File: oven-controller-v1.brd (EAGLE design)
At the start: 61 x 57.1 mm, 22 parts, among them Q1 IRFL310, U1 ARDUINO_SHIELDLONGPADS

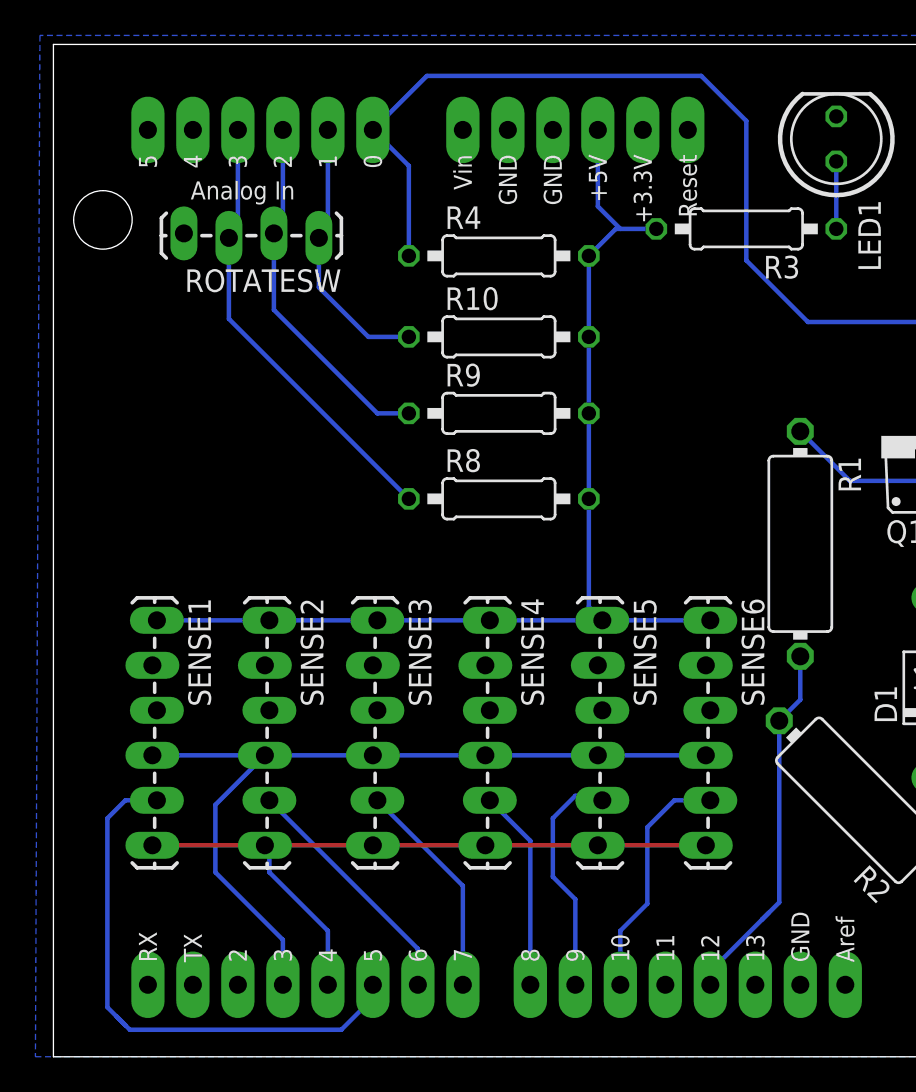
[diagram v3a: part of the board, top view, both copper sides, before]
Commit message: Final board routed.
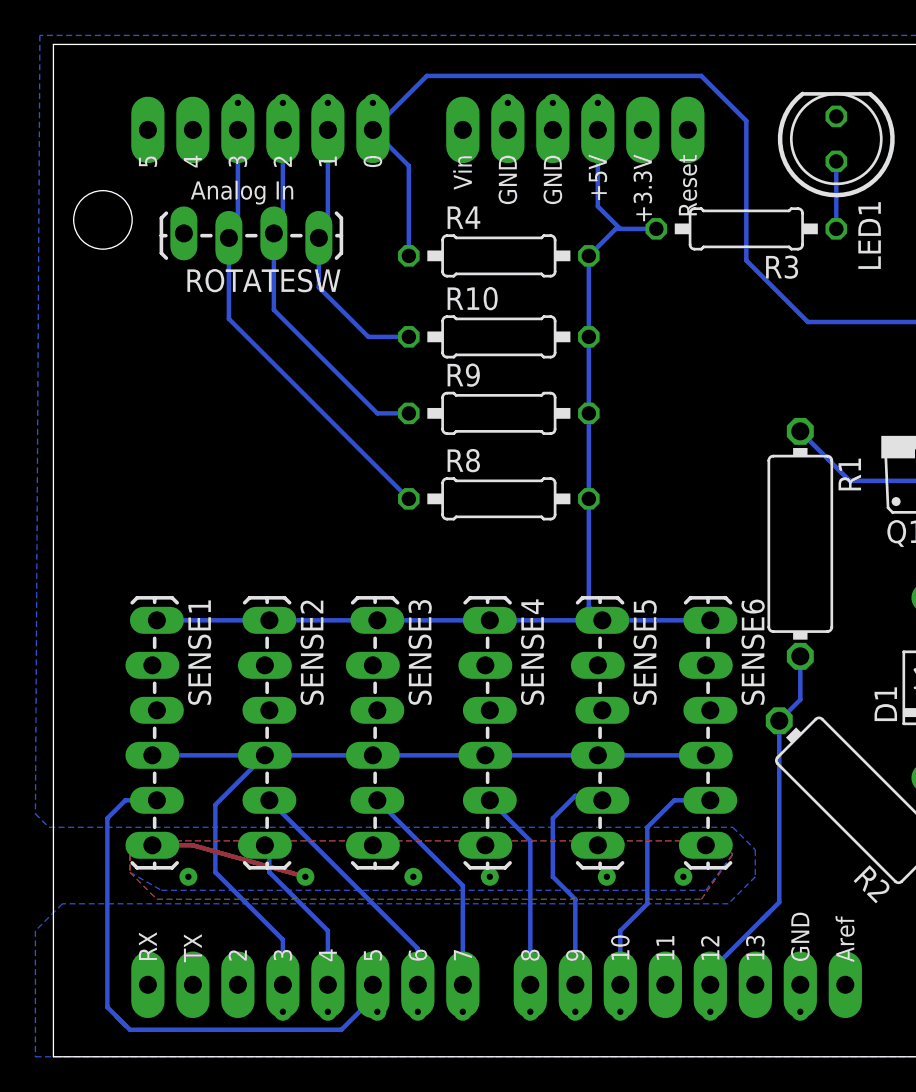
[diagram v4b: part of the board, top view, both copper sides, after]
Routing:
- net SCLK_PIN4: track 40.8 -> 20.0 mm, vias 0 -> 7
- net A1: track 15.3 -> 16.9 mm, vias 0 -> 1
- net SDA_PIN3: track 46.9 -> 48.5 mm, vias 0 -> 1
- net PIN12: track 21.2 -> 22.7 mm, vias 0 -> 1
- net CS_PIN9: track 13.3 -> 14.9 mm, vias 0 -> 1
- net CS_PIN8: track 11.4 -> 12.9 mm, vias 0 -> 1
- net CS_PIN7: track 12.4 -> 13.9 mm, vias 0 -> 1
- net A3: track 25.2 -> 26.8 mm, vias 0 -> 1
- net A2: track 20.4 -> 21.9 mm, vias 0 -> 1
- net A0: track 55.9 -> 57.4 mm, vias 0 -> 1
- net 5V: track 62.7 -> 64.2 mm, vias 0 -> 1
- net CS_PIN6: track 13.9 -> 15.4 mm, vias 0 -> 1
- net CS_PIN10: track 13.7 -> 15.2 mm, vias 0 -> 1
- net CS_PIN5: track 31.6 -> 32.6 mm, vias 0 -> 1
- added copper zone on layer 1, net SCLK_PIN4
- added copper zone on layer 16, net SCLK_PIN4
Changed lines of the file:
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@@
 <grid distance="0.01" unitdist="inch" unit="inch" style="dots" multiple="1" display="yes" altdistance="0.001" altunitdist="inch" altunit="inch"/>
 <layers>
-<layer number="1" name="Top" color="4" fill="1" visible="yes" active="yes"/>
+<layer number="1" name="Top" color="4" fill="1" visible="no" active="yes"/>
 <layer number="2" name="Route2" color="1" fill="3" visible="no" active="no"/>
 <layer number="3" name="Route3" color="4" fill="3" visible="no" active="no"/>
@@
 <vertex x="61.214" y="57.658"/>
 <vertex x="-0.762" y="57.658"/>
+<vertex x="-1.016" y="13.716"/>
+<vertex x="-0.254" y="12.954"/>
+<vertex x="38.354" y="12.954"/>
+<vertex x="39.624" y="11.684"/>
+<vertex x="39.624" y="10.16"/>
+<vertex x="38.1" y="8.636"/>
+<vertex x="0.508" y="8.636"/>
+<vertex x="-1.016" y="7.112"/>
 <vertex x="-1.016" y="0"/>
 <vertex x="60.96" y="0"/>
 </polygon>
+<via x="25.654" y="53.848" extent="1-16" drill="0.3556" diameter="1.016"/>
+<via x="28.194" y="53.848" extent="1-16" drill="0.3556" diameter="1.016"/>
+<via x="42.164" y="2.54" extent="1-16" drill="0.3556" diameter="1.016"/>
 </signal>
 <signal name="PIN12">
@@
 <wire x1="40.975871875" y1="18.968125" x2="40.975871875" y2="8.717871875" width="0.254" layer="16"/>
 <wire x1="40.975871875" y1="8.717871875" x2="40.005" y2="7.747" width="0.254" layer="16"/>
+<via x="37.084" y="2.54" extent="1-16" drill="0.3556" diameter="1.016"/>
+<wire x1="37.084" y1="2.54" x2="37.084" y2="4.064" width="0.254" layer="16"/>
 </signal>
 <signal name="N$2">
@@
 <wire x1="24.384" y1="17.018" x2="30.734" y2="17.018" width="0.254" layer="16"/>
 <wire x1="30.734" y1="17.018" x2="36.83" y2="17.018" width="0.254" layer="16"/>
+<via x="12.954" y="2.54" extent="1-16" drill="0.3556" diameter="1.016"/>
+<wire x1="12.954" y1="2.54" x2="12.954" y2="4.064" width="0.254" layer="16"/>
 </signal>
 <signal name="SCLK_PIN4">
@@
 <contactref element="SENSE6" pad="6"/>
 <contactref element="U1" pad="D4"/>
-<wire x1="5.588" y1="11.938" x2="11.938" y2="11.938" width="0.254" layer="1"/>
-<wire x1="11.938" y1="11.938" x2="18.034" y2="11.938" width="0.254" layer="1"/>
-<wire x1="18.034" y1="11.938" x2="24.384" y2="11.938" width="0.254" layer="1"/>
-<wire x1="24.384" y1="11.938" x2="30.734" y2="11.938" width="0.254" layer="1"/>
 <wire x1="30.734" y1="11.938" x2="30.988" y2="11.938" width="0.254" layer="1"/>
-<wire x1="30.734" y1="11.938" x2="36.83" y2="11.938" width="0.254" layer="1"/>
 <wire x1="15.494" y1="4.064" x2="15.494" y2="7.112" width="0.254" layer="16"/>
 <wire x1="15.494" y1="7.112" x2="12.192" y2="10.414" width="0.254" layer="16"/>
 <wire x1="12.192" y1="10.414" x2="12.192" y2="11.684" width="0.254" layer="16"/>
 <wire x1="12.192" y1="11.684" x2="11.938" y2="11.938" width="0.254" layer="16"/>
+<polygon width="0.254" layer="1">
+<vertex x="4.318" y="11.938"/>
+<vertex x="4.318" y="10.414"/>
+<vertex x="5.842" y="8.89"/>
+<vertex x="36.576" y="8.89"/>
+<vertex x="38.354" y="11.43"/>
+<vertex x="37.592" y="12.192"/>
+<vertex x="4.572" y="12.192"/>
+</polygon>
+<via x="14.224" y="10.16" extent="1-16" drill="0.3556" diameter="1.016"/>
+<wire x1="5.588" y1="11.938" x2="7.874" y2="11.938" width="0.254" layer="1"/>
+<wire x1="7.874" y1="11.938" x2="14.224" y2="10.16" width="0.254" layer="1"/>
+<polygon width="0.254" layer="16">
+<vertex x="4.318" y="11.938"/>
+<vertex x="4.318" y="10.414"/>
+<vertex x="6.096" y="9.398"/>
+<vertex x="36.83" y="9.398"/>
+<vertex x="38.354" y="11.43"/>
+<vertex x="37.592" y="12.192"/>
+<vertex x="4.572" y="12.192"/>
+</polygon>
+<via x="15.494" y="2.54" extent="1-16" drill="0.3556" diameter="1.016"/>
+<wire x1="15.494" y1="2.54" x2="15.494" y2="4.064" width="0.254" layer="16"/>
+<via x="7.62" y="10.16" extent="1-16" drill="0.3556" diameter="1.016"/>
+<via x="20.32" y="10.16" extent="1-16" drill="0.3556" diameter="1.016"/>
+<via x="24.638" y="10.16" extent="1-16" drill="0.3556" diameter="1.016"/>
+<via x="31.242" y="10.16" extent="1-16" drill="0.3556" diameter="1.016"/>
+<via x="35.56" y="10.16" extent="1-16" drill="0.3556" diameter="1.016"/>
 </signal>
 <signal name="CS_PIN10">
@@
 <wire x1="33.528" y1="8.636" x2="32.004" y2="7.112" width="0.254" layer="16"/>
 <wire x1="32.004" y1="7.112" x2="32.004" y2="4.064" width="0.254" layer="16"/>
+<via x="32.004" y="2.54" extent="1-16" drill="0.3556" diameter="1.016"/>
+<wire x1="32.004" y1="2.54" x2="32.004" y2="4.064" width="0.254" layer="16"/>
 </signal>
 <signal name="CS_PIN6">
@@
 <wire x1="20.574" y1="4.064" x2="20.574" y2="6.096" width="0.254" layer="16"/>
 <wire x1="20.574" y1="6.096" x2="12.192" y2="14.478" width="0.254" layer="16"/>
+<via x="20.574" y="2.54" extent="1-16" drill="0.3556" diameter="1.016"/>
+<wire x1="20.574" y1="4.064" x2="20.574" y2="2.54" width="0.254" layer="16"/>
 </signal>
 <signal name="CS_PIN8">
@@
 <wire x1="26.924" y1="4.064" x2="26.924" y2="12.192" width="0.254" layer="16"/>
 <wire x1="26.924" y1="12.192" x2="24.638" y2="14.478" width="0.254" layer="16"/>
+<via x="26.924" y="2.54" extent="1-16" drill="0.3556" diameter="1.016"/>
+<wire x1="26.924" y1="2.54" x2="26.924" y2="4.064" width="0.254" layer="16"/>
 </signal>
 <signal name="CS_PIN7">
@@
 <wire x1="23.114" y1="4.064" x2="23.114" y2="9.652" width="0.254" layer="16"/>
 <wire x1="23.114" y1="9.652" x2="18.288" y2="14.478" width="0.254" layer="16"/>
+<via x="23.114" y="2.54" extent="1-16" drill="0.3556" diameter="1.016"/>
+<wire x1="23.114" y1="2.54" x2="23.114" y2="4.064" width="0.254" layer="16"/>
 </signal>
 <signal name="CS_PIN9">
@@
 <wire x1="29.464" y1="14.732" x2="30.734" y2="14.732" width="0.254" layer="16"/>
 <wire x1="30.734" y1="14.732" x2="30.988" y2="14.478" width="0.254" layer="16"/>
+<via x="29.464" y="2.54" extent="1-16" drill="0.3556" diameter="1.016"/>
+<wire x1="29.464" y1="2.54" x2="29.464" y2="4.064" width="0.254" layer="16"/>
 </signal>
 <signal name="CS_PIN5">
@@
 <wire x1="3.048" y1="13.462" x2="3.048" y2="2.794" width="0.254" layer="16"/>
 <wire x1="3.048" y1="2.794" x2="4.064" y2="1.778" width="0.254" layer="16"/>
+<via x="18.288" y="2.54" extent="1-16" drill="0.3556" diameter="1.016"/>
+<wire x1="18.288" y1="2.54" x2="18.034" y2="2.54" width="0.254" layer="16"/>
+<wire x1="18.034" y1="2.54" x2="18.034" y2="3.302" width="0.254" layer="16"/>
 </signal>
 <signal name="N$11">
@@
 <wire x1="20.066" y1="45.212" x2="20.066" y2="50.292" width="0.254" layer="16"/>
 <wire x1="20.066" y1="50.292" x2="18.034" y2="52.324" width="0.254" layer="16"/>
+<via x="18.034" y="53.848" extent="1-16" drill="0.3556" diameter="1.016"/>
+<wire x1="18.034" y1="53.848" x2="18.034" y2="52.324" width="0.254" layer="16"/>
 </signal>
 <signal name="N$10">
@@
 <wire x1="17.78" y1="40.64" x2="14.986" y2="43.434" width="0.254" layer="16"/>
 <wire x1="14.986" y1="43.434" x2="14.986" y2="46.228" width="0.254" layer="16"/>
+<via x="15.494" y="53.848" extent="1-16" drill="0.3556" diameter="1.016"/>
+<wire x1="15.494" y1="53.848" x2="15.494" y2="52.324" width="0.254" layer="16"/>
 </signal>
 <signal name="A2">
@@
 <wire x1="18.288" y1="36.322" x2="12.446" y2="42.164" width="0.254" layer="16"/>
 <wire x1="12.446" y1="42.164" x2="12.446" y2="46.482" width="0.254" layer="16"/>
+<via x="12.954" y="53.848" extent="1-16" drill="0.3556" diameter="1.016"/>
+<wire x1="12.954" y1="52.324" x2="12.954" y2="53.848" width="0.254" layer="16"/>
 </signal>
 <signal name="A3">
@@
 <wire x1="9.906" y1="46.228" x2="9.906" y2="41.656" width="0.254" layer="16"/>
 <wire x1="9.906" y1="41.656" x2="20.066" y2="31.496" width="0.254" layer="16"/>
+<via x="10.414" y="53.848" extent="1-16" drill="0.3556" diameter="1.016"/>
+<wire x1="10.414" y1="53.848" x2="10.414" y2="52.324" width="0.254" layer="16"/>
 </signal>
 <signal name="5V">
@@
 <wire x1="30.226" y1="31.496" x2="30.226" y2="25.4" width="0.254" layer="16"/>
 <wire x1="30.226" y1="25.4" x2="30.988" y2="24.638" width="0.254" layer="16"/>
+<via x="30.734" y="53.848" extent="1-16" drill="0.3556" diameter="1.016"/>
+<wire x1="30.734" y1="53.848" x2="30.734" y2="52.324" width="0.254" layer="16"/>
 </signal>
 <signal name="VIN">
